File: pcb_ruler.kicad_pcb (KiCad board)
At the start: 2 copper layers, 160 x 38 mm, 35 parts

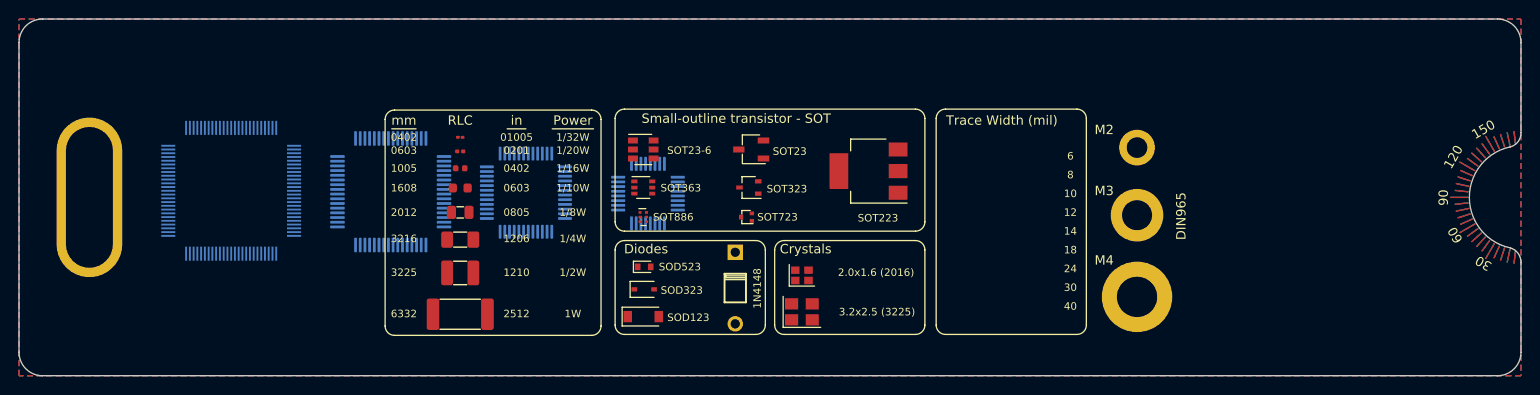
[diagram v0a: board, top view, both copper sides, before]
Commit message: more rounding and ruler to edge
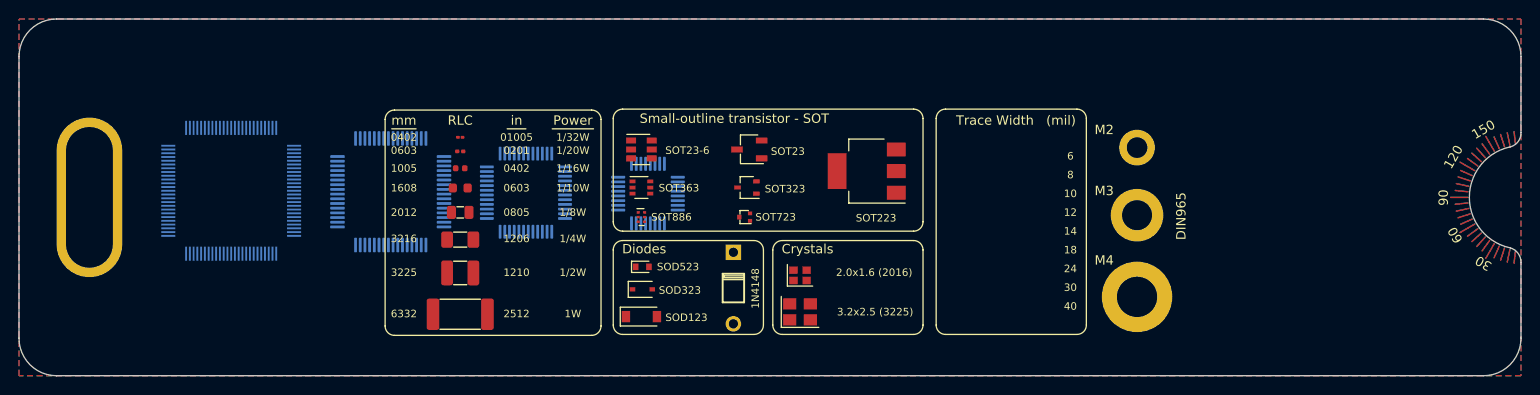
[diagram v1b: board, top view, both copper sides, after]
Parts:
- moved REF** 0.20 mm to (183.2, 131.2)
- moved REF** 0.20 mm to (183.2, 127.3)
- moved Ref** 0.20 mm to (176.1, 128.7)
- moved ? 0.20 mm to (166.3, 113.9)
- moved REF** 0.20 mm to (166.3, 121.1)
- moved REF** 0.20 mm to (177.3, 121.1)
- moved REF** 0.20 mm to (166.4, 126.4)
- moved REF** 0.20 mm to (166.4, 128.8)
- moved REF** 0.20 mm to (166.3, 131.7)
- moved REF** 0.20 mm to (190.3, 116.2)
- moved REF** 0.20 mm to (177.6, 118.0)
- moved REF** 0.20 mm to (166.3, 118.0)
- moved REF** 0.20 mm to (177.8, 113.9)
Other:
- outline, holes or cut-outs redrawn
- board text added: "CASE PCB Ruler v.1.1 D. Quach 2020"
- board text removed: "CASE PCB Ruler v1.0 D. Quach 2020"
